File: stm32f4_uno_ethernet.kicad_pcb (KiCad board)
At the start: 2 copper layers, 68.6 x 53.3 mm, 55 parts, among them J104 STM32 GPIO, J106 Power, J107 Ethernet, J110 Analog, J111 Conn_01x04, J201 RJ45-TH_B-1-1, U201 SRV05-4, U202 LAN8742A, Y201 25MHz

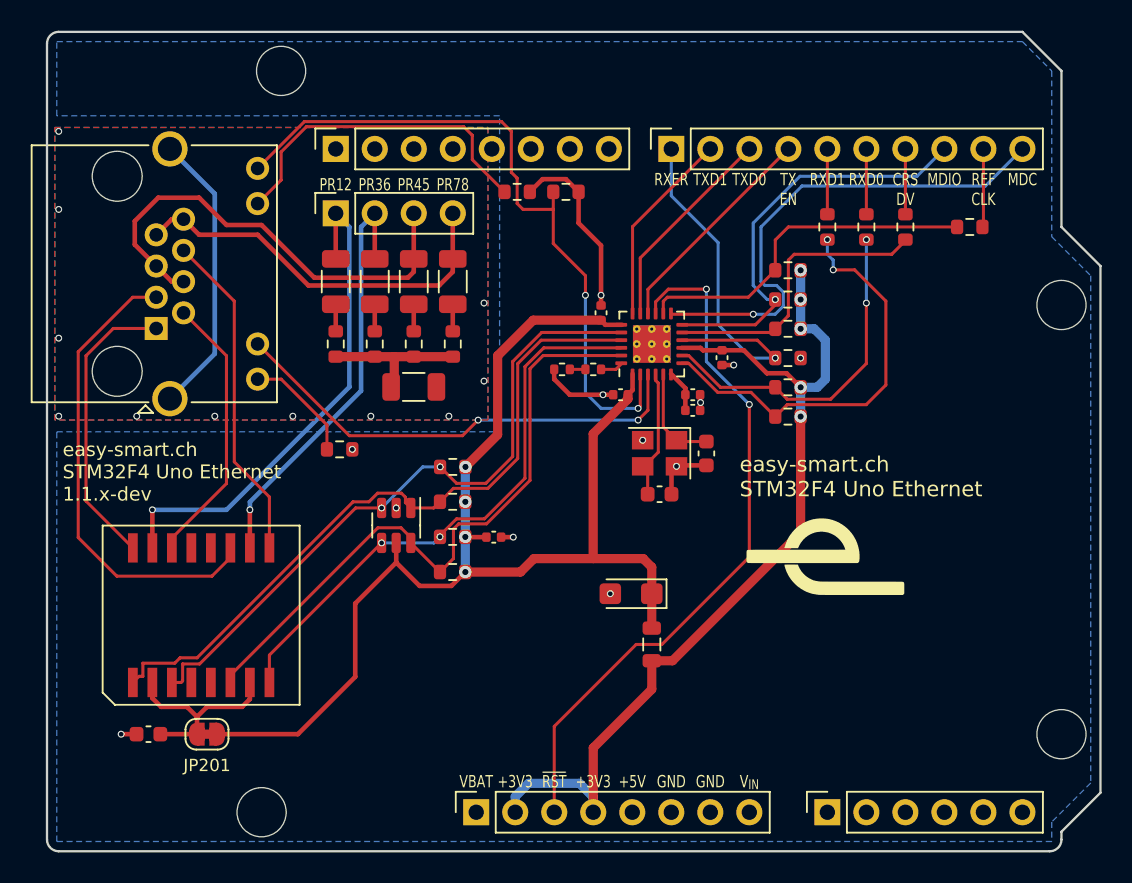
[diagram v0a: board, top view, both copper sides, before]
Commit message: #8 Add all pin sockets on ethernet
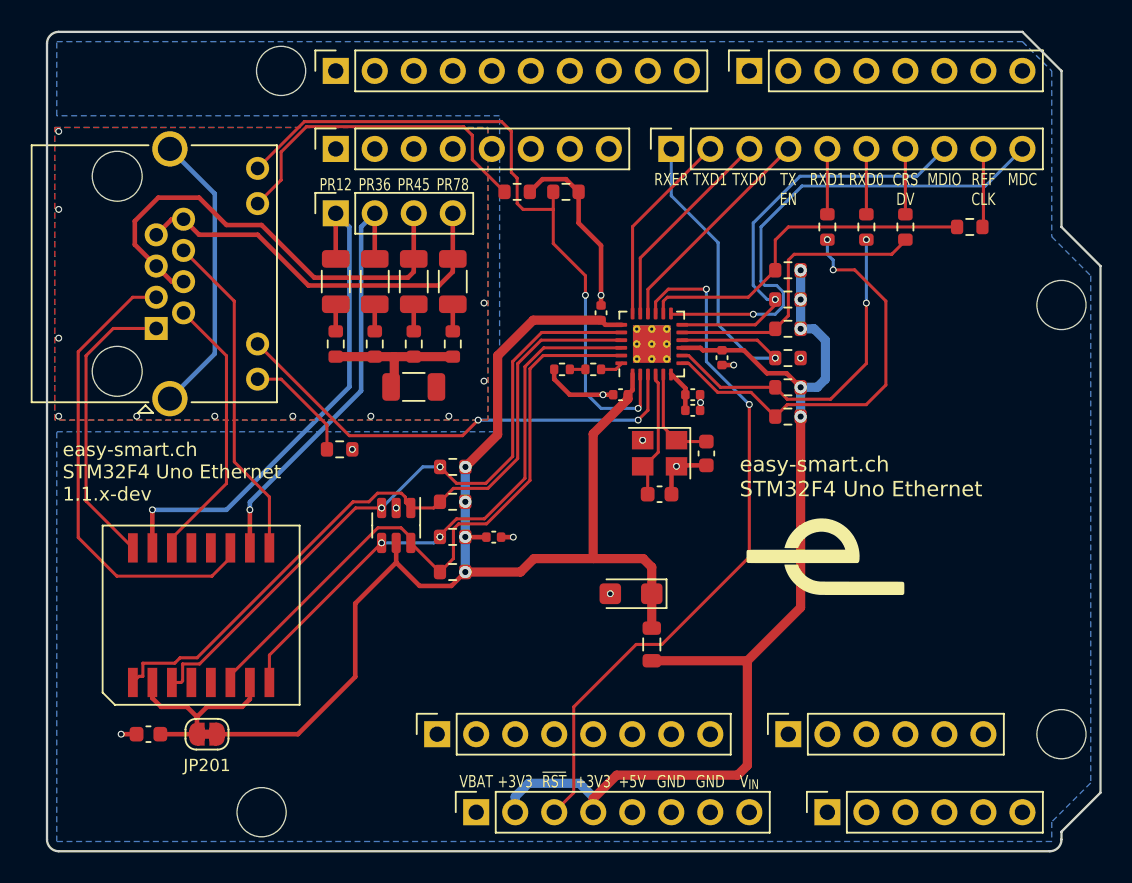
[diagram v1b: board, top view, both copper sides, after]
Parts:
- added J102: Digital/PWM, Connector_PinSocket_2.54mm:PinSocket_1x10_P2.54mm_Vertical, F.Cu at (118.8, 49.2)
- added J105: STM32 GPIO, Connector_PinSocket_2.54mm:PinSocket_1x08_P2.54mm_Vertical, F.Cu at (125.4, 92.4)
- added J108: STM32 GPIO, Connector_PinSocket_2.54mm:PinSocket_1x06_P2.54mm_Vertical, F.Cu at (148.3, 92.4)
- added J109: Digital/PWM, Connector_PinSocket_2.54mm:PinSocket_1x08_P2.54mm_Vertical, F.Cu at (145.7, 49.2)
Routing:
- net +3V3: track 60.8 -> 70.8 mm
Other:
- board text added: "ICSP"
- board text removed: "locked"

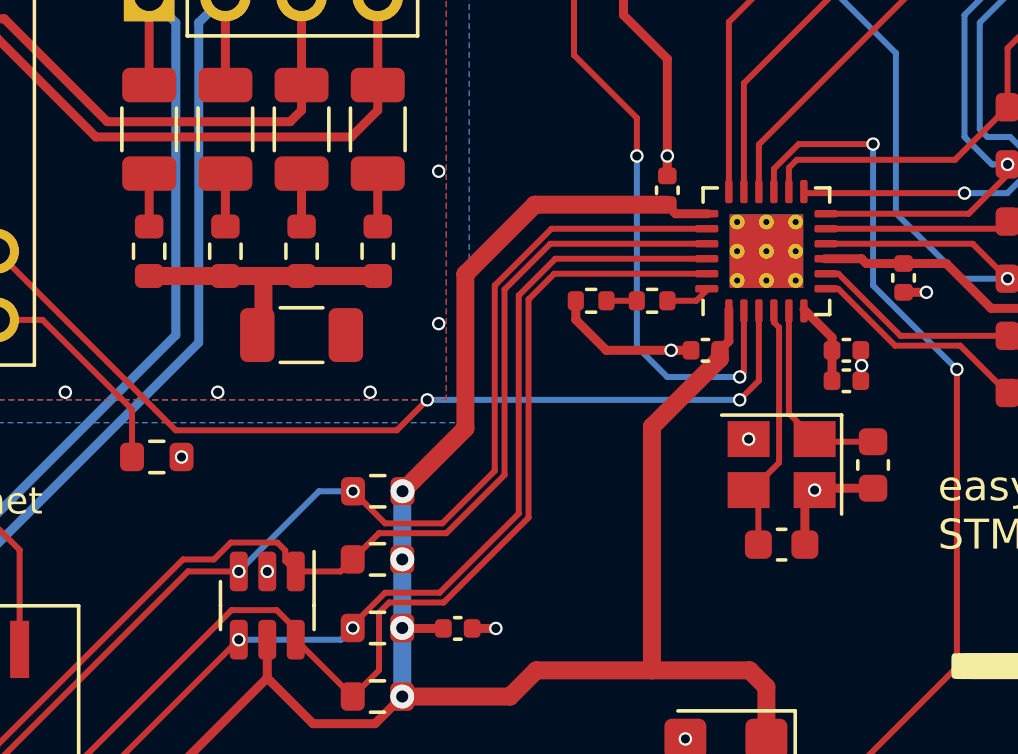
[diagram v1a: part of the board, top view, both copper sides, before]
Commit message: #7 Change ethernet signal transformer
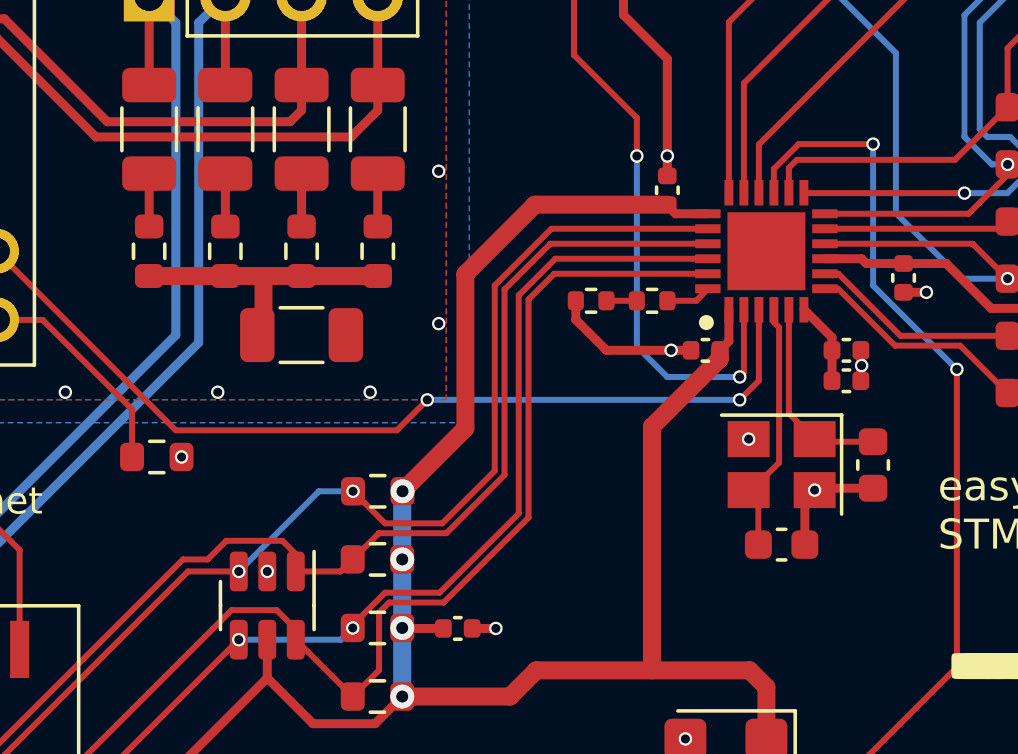
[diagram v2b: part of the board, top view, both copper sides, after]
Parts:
- U202: footprint Package_DFN_QFN:VQFN-24-1EP_4x4mm_P0.5mm_EP2.45x2.45mm_ThermalVias -> #IC:LAN8742AI-CZ-TR
